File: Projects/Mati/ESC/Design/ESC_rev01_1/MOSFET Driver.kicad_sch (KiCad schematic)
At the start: 0 parts

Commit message: Uptade 04
DRV8302 Motor Driver
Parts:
- added C18: 120p, symbol Device:C
- added C19: 6n8, symbol Device:C
- added C20, C22, C23, C24: 2u2, symbol Device:C
- added C21: 22n, symbol Device:C
- added C25, C26, C27, C28, C29, C30, C31, C32, C33: 10u, symbol Device:C
- added C34, C35, C36: 220n, symbol Device:C
- added C37: 100u, symbol Device:C
- added C38: 100n, symbol Device:C
- added D4, D5: D_Schottky, symbol Device:D_Schottky
- added L1: L, symbol Device:L
- added R11, R17, R18, R19, R20, R21, R22, R23, R24: 205k, symbol Device:R
- added R12: 16k2, symbol Device:R
- added R13: 31k6, symbol Device:R
- added R14, R15: 10k, symbol Device:R
- added R16: 1M, symbol Device:R
- added U2: DRV8302DCAR, DCA56_6P35X3P61, symbol DRV8302:DRV8302DCAR
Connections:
- new net: C34.1, U2.38 (BST_C)
- new net: C36.1, U2.48 (BST_A)
- new net: C24.1, U2.24 (REF), U2.27 (AVDD)
- new net: C18.1, R11.1, R12.1, U2.1 (RT_CLK)
- new net: C19.1, R12.2
- new net: C35.1, U2.43 (BST_B)
- new net: C37.2, D5.2 (A), L1.2
- new net: C20.1, C22.1, U2.13 (GVDD)
- new net: R15.1, U2.7 (DTC)
- new net: C23.1, U2.23 (DVDD)
- new net: R13.2, R14.1, U2.3 (VSENSE)
- new net: C38.2, D4.1 (K), L1.1, U2.50 (PH), U2.51 (PH)
- new net: R16.1, U2.49 (BIAS)
- new net: C18.2, C19.2, U2.2 (COMP)
- new net: C21.2, U2.14 (CP1)
- new net: C21.1, U2.15 (CP2)
- new net: C38.1, U2.52 (BST_BK)
- new net +5V: D5.1 (K), R14.2
- new net +VDC: C25.1, C26.1, C27.1, C28.1, C29.1, C30.1, C31.1, C32.1, C33.1, R23.1, U2.29 (PVDD1), U2.56 (SS_TR)
- new net CS: U2.8 (M_PWM)
- new net EN_GATE: U2.16 (EN_GATE)
- new net GH_A: U2.47 (GH_A)
- new net GH_B: U2.42 (GH_B)
- new net GH_C: U2.37 (GH_C)
- new net GL_A: U2.45 (GL_A)
- new net GL_B: U2.40 (GL_B)
- new net GL_C: U2.35 (GL_C)
- new net GND: C20.2, C22.2, C23.2, C24.2, C25.2, C26.2, C27.2, C28.2, C29.2, C30.2, C31.2, C32.2, C33.2, C37.1, D4.2 (A), R11.2, R13.1, R15.2, R16.2, R18.2, R20.2, R22.2, R24.2, U2.28 (AGND), U2.57 (EPAD)
- new net INH_A: U2.17 (INH_A)
- new net INH_B: U2.19 (INH_B)
- new net INH_C: U2.21 (INH_C)
- new net INL_A: U2.18 (INL_A)
- new net INL_B: U2.20 (INL_B)
- new net INL_C: U2.22 (INL_C)
- new net SCLK: U2.11 (OC_ADJ)
- new net SDD: U2.10 (GAIN)
- new net SDI: U2.9 (M_OC)
- new net SENS_A: R17.2, R18.1
- new net SENS_B: R19.2, R20.1
- new net SENS_C: R21.2, R22.1
- new net SENS_SUPPLY: R23.2, R24.1
- new net SH_A: C36.2, R17.1, U2.46 (SH_A)
- new net SH_B: C35.2, R19.1, U2.41 (SH_B)
- new net SH_C: C34.2, R21.1, U2.36 (SH_C)
- new net SL_A: U2.44 (SL_A)
- new net SL_B: U2.39 (SL_B)
- new net SL_C: U2.34 (SL_C)
- new net SN1: U2.33 (SN1)
- new net SN2: U2.31 (SN2)
- new net SP1: U2.32 (SP1)
- new net SP2: U2.30 (SP2)
- no-connect marks 0 -> 5

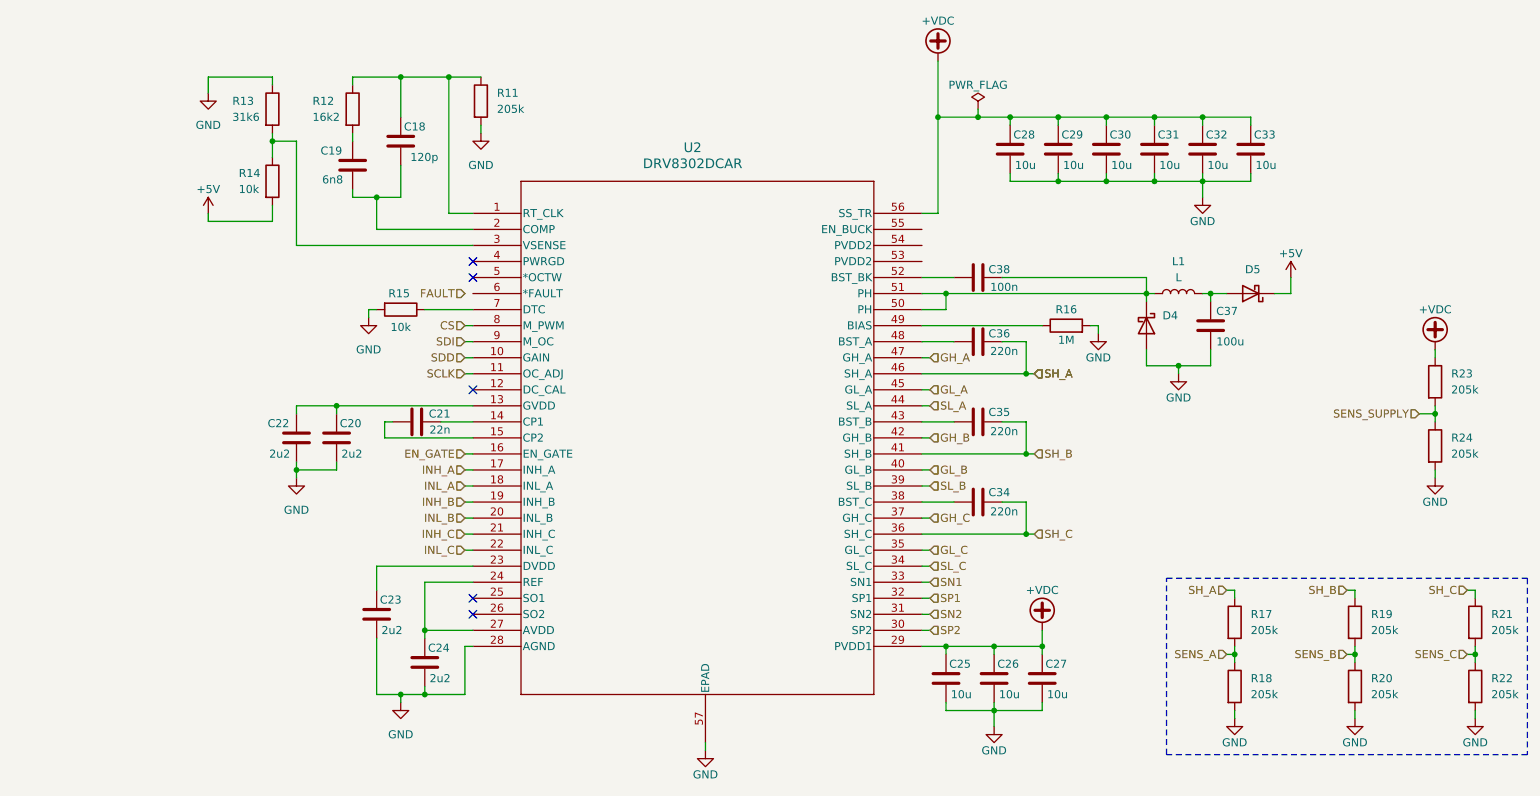
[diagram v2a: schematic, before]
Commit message: Update 05
Transistors & ESC Motor Phases Schematics
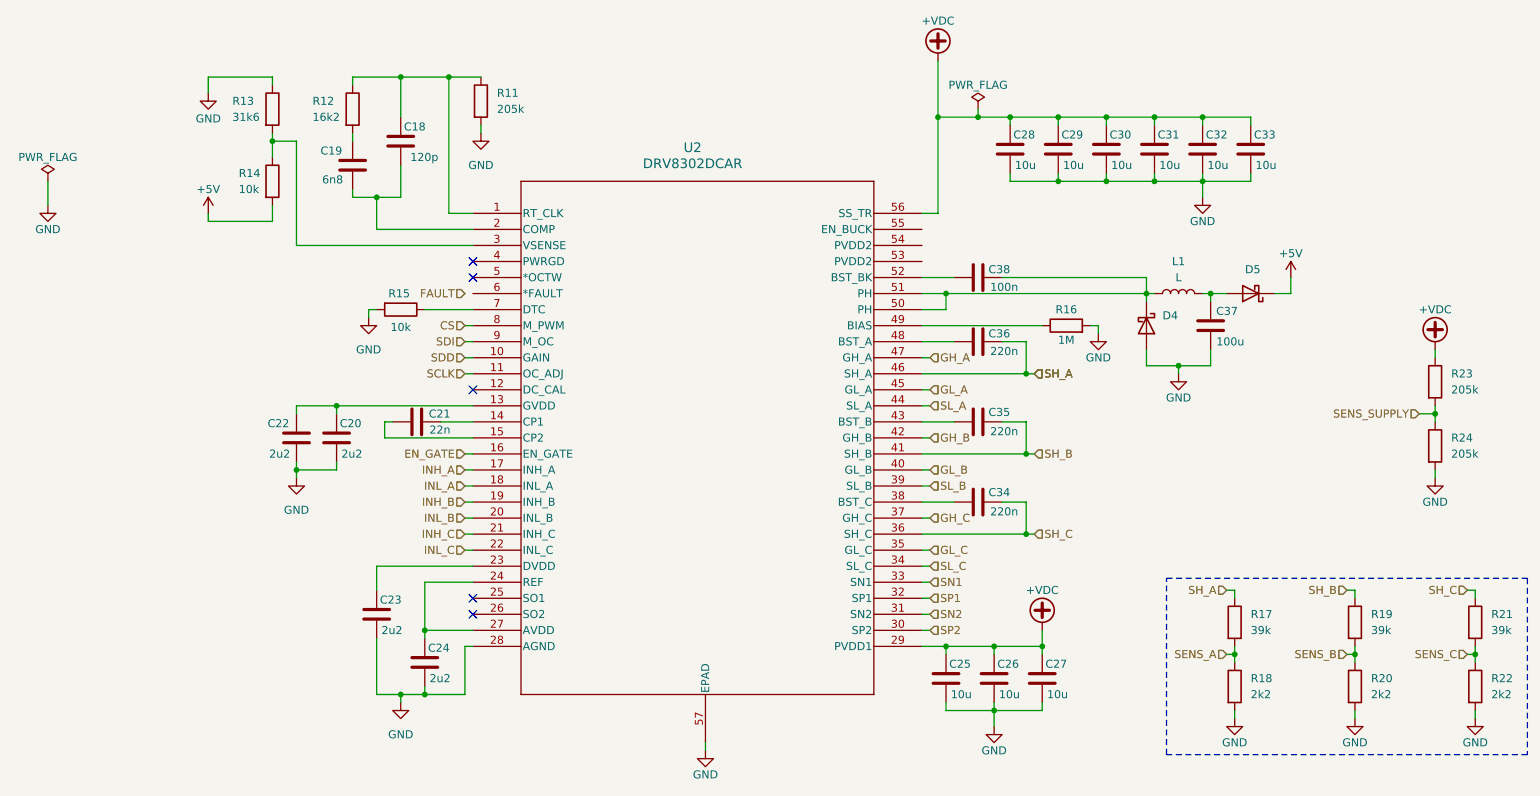
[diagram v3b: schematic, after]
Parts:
- R17, R19, R21: value 205k -> 39k
- R18, R20, R22: value 205k -> 2k2
